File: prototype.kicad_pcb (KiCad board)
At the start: 2 copper layers, 101.5 x 83 mm, 7 parts, among them CON1 SNES-CONN, IC1 SN74LVC4245A, IC2 SN74LVC4245A, IC3 SN74LVC4245A, IC4 SN74LVC4245A

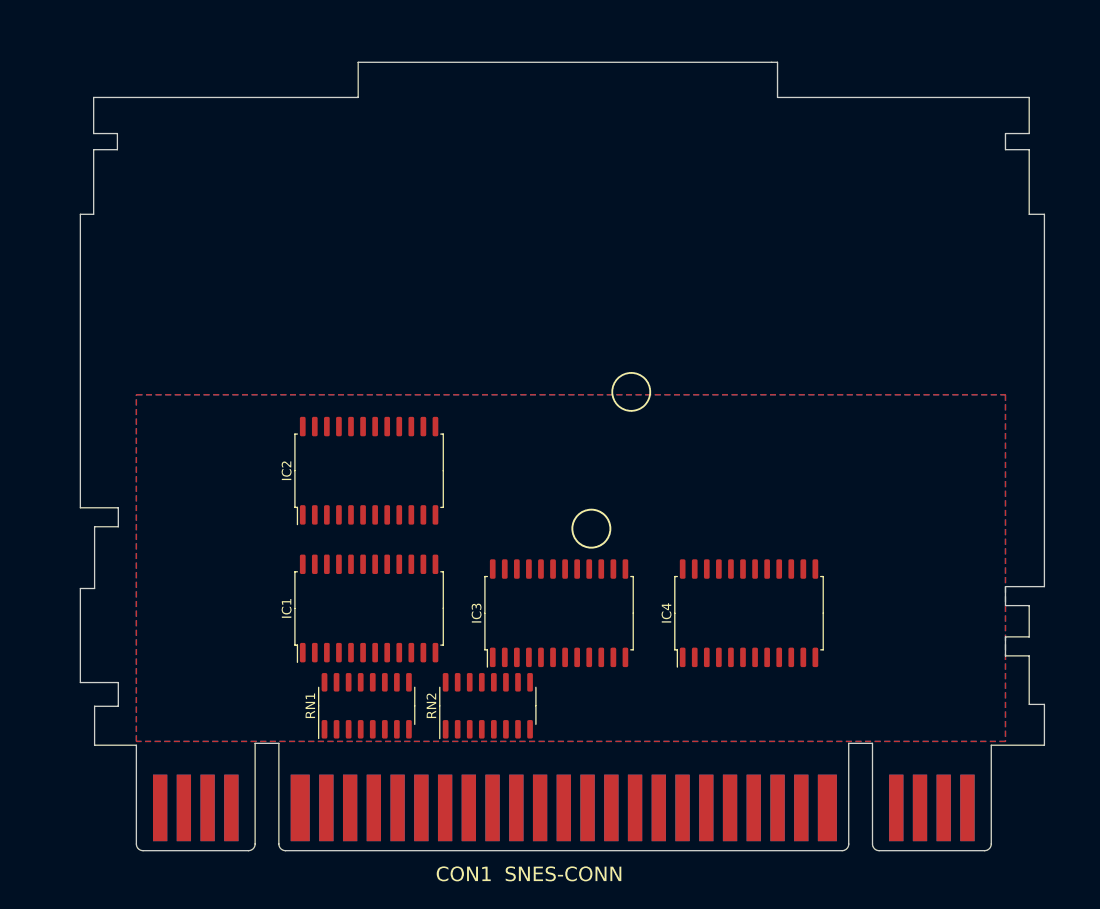
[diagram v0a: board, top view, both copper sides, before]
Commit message: Add resistor networks in between edge connectors and level shifters
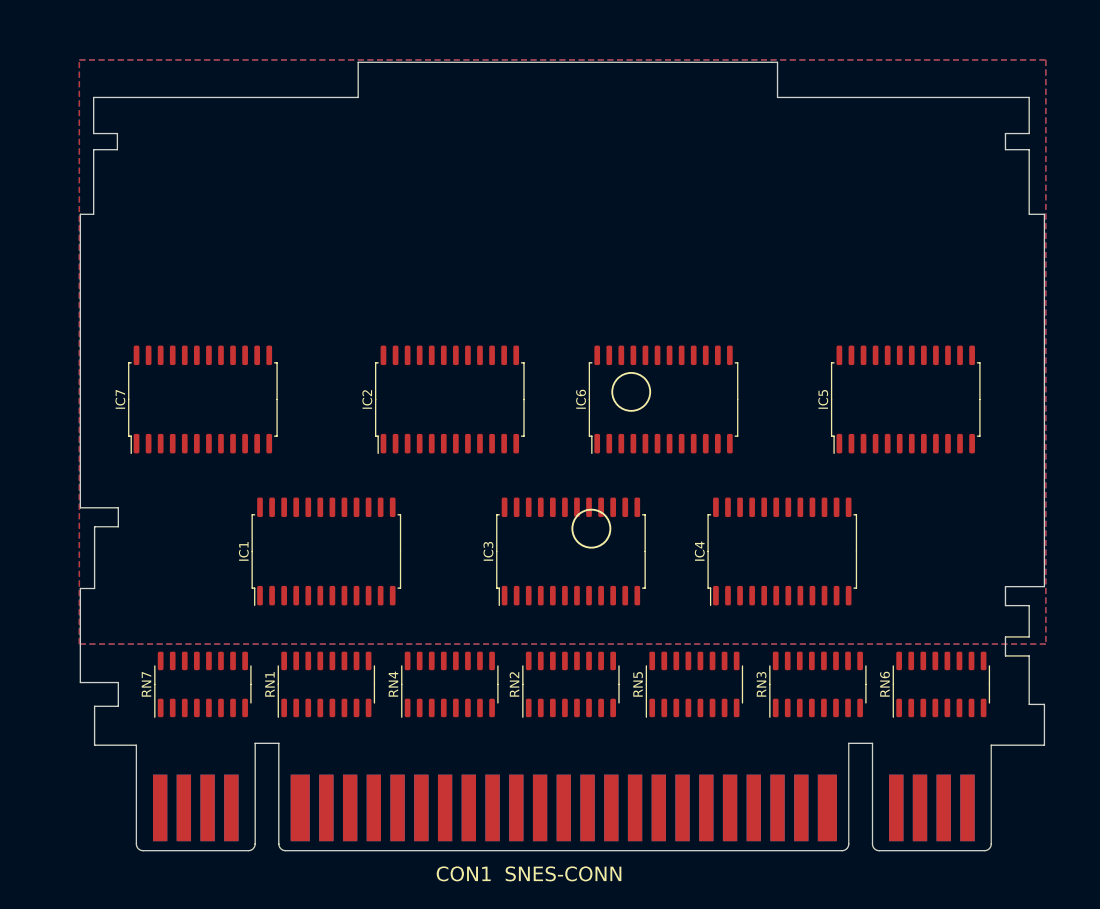
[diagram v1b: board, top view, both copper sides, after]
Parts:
- added IC5: SN74LVC4245A, Package_SO:SOIC-24W_7.5x15.4mm_P1.27mm, F.Cu at (187.0, 87.5)
- added IC6: SN74LVC4245A, Package_SO:SOIC-24W_7.5x15.4mm_P1.27mm, F.Cu at (161.5, 87.5)
- added IC7: SN74LVC4245A, Package_SO:SOIC-24W_7.5x15.4mm_P1.27mm, F.Cu at (113.0, 87.5)
- added RN3: R_Pack08, Package_SO:SOIC-16_3.9x9.9mm_P1.27mm, F.Cu at (177.8, 117.5)
- added RN4: R_Pack08, Package_SO:SOIC-16_3.9x9.9mm_P1.27mm, F.Cu at (139.0, 117.5)
- added RN5: R_Pack08, Package_SO:SOIC-16_3.9x9.9mm_P1.27mm, F.Cu at (164.8, 117.5)
- added RN6: R_Pack08, Package_SO:SOIC-16_3.9x9.9mm_P1.27mm, F.Cu at (190.8, 117.5)
- added RN7: R_Pack08, Package_SO:SOIC-16_3.9x9.9mm_P1.27mm, F.Cu at (113.0, 117.5)
- moved IC2 11.3 mm to (139.0, 87.5)
- moved RN2 9.03 mm to (151.8, 117.5)
- moved IC1 7.50 mm to (126.0, 103.5)
- moved IC4 7.38 mm to (174.0, 103.5)
- moved IC3 6.62 mm to (151.8, 103.5)
- moved RN1 4.81 mm to (126.0, 117.5)
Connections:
- CON1 pad 1: unconnected-(CON1-Pad1) -> Net-(RN7-Pad1)
- CON1 pad 14: A3 -> Net-(CON1-Pad14)
- CON1 pad 15: A2 -> Net-(CON1-Pad15)
- CON1 pad 16: A1 -> Net-(CON1-Pad16)
- CON1 pad 17: A0 -> Net-(CON1-Pad17)
- CON1 pad 18: unconnected-(CON1-Pad18) -> Net-(CON1-Pad18)
- CON1 pad 19: D0 -> Net-(CON1-Pad19)
- CON1 pad 2: unconnected-(CON1-Pad2) -> Net-(RN7-Pad2)
- CON1 pad 20: D1 -> Net-(CON1-Pad20)
- CON1 pad 21: D2 -> Net-(CON1-Pad21)
- CON1 pad 22: D3 -> Net-(CON1-Pad22)
- CON1 pad 23: unconnected-(CON1-Pad23) -> Net-(CON1-Pad23)
- CON1 pad 24: unconnected-(CON1-Pad24) -> Net-(CON1-Pad24)
- CON1 pad 25: unconnected-(CON1-Pad25) -> Net-(CON1-Pad25)
- CON1 pad 26: unconnected-(CON1-Pad26) -> Net-(CON1-Pad26)
- CON1 pad 28: unconnected-(CON1-Pad28) -> Net-(CON1-Pad28)
- CON1 pad 29: unconnected-(CON1-Pad29) -> Net-(CON1-Pad29)
- CON1 pad 3: unconnected-(CON1-Pad3) -> Net-(RN7-Pad3)
- CON1 pad 30: unconnected-(CON1-Pad30) -> Net-(CON1-Pad30)
- CON1 pad 32: unconnected-(CON1-Pad32) -> Net-(RN7-Pad5)
- CON1 pad 33: unconnected-(CON1-Pad33) -> Net-(RN7-Pad6)
- CON1 pad 34: unconnected-(CON1-Pad34) -> Net-(RN7-Pad7)
- CON1 pad 35: unconnected-(CON1-Pad35) -> Net-(RN7-Pad8)
- CON1 pad 4: unconnected-(CON1-Pad4) -> Net-(RN7-Pad4)
- CON1 pad 45: A20 -> Net-(CON1-Pad45)
- CON1 pad 46: A21 -> Net-(CON1-Pad46)
- CON1 pad 47: A22 -> Net-(CON1-Pad47)
- CON1 pad 48: A23 -> Net-(CON1-Pad48)
- CON1 pad 49: unconnected-(CON1-Pad49) -> Net-(CON1-Pad49)
- CON1 pad 50: D4 -> Net-(CON1-Pad50)
- CON1 pad 51: D5 -> Net-(CON1-Pad51)
- CON1 pad 52: D6 -> Net-(CON1-Pad52)
- CON1 pad 53: D7 -> Net-(CON1-Pad53)
- CON1 pad 54: unconnected-(CON1-Pad54) -> Net-(CON1-Pad54)
- CON1 pad 55: unconnected-(CON1-Pad55) -> Net-(CON1-Pad55)
- CON1 pad 56: unconnected-(CON1-Pad56) -> Net-(CON1-Pad56)
- CON1 pad 57: unconnected-(CON1-Pad57) -> Net-(CON1-Pad57)
- CON1 pad 59: unconnected-(CON1-Pad59) -> Net-(CON1-Pad59)
- CON1 pad 60: unconnected-(CON1-Pad60) -> Net-(CON1-Pad60)
- CON1 pad 61: unconnected-(CON1-Pad61) -> Net-(CON1-Pad61)
- IC1 pad 2: A12 -> GND
- IC2 pad 2: unconnected-(IC2-Pad2) -> GND
- IC3 pad 2: unconnected-(IC3-Pad2) -> GND
- RN1 pad 1: A11 -> Net-(CON1-Pad6)
- RN1 pad 10: Net-(CON1-Pad12) -> A5
- RN1 pad 11: Net-(CON1-Pad11) -> A6
- RN1 pad 12: Net-(CON1-Pad10) -> A7
- RN1 pad 13: Net-(CON1-Pad9) -> A8
- RN1 pad 14: Net-(CON1-Pad8) -> A9
- RN1 pad 15: Net-(CON1-Pad7) -> A10
- RN1 pad 16: Net-(CON1-Pad6) -> A11
- RN1 pad 2: A10 -> Net-(CON1-Pad7)
- RN1 pad 3: A9 -> Net-(CON1-Pad8)
- RN1 pad 4: A8 -> Net-(CON1-Pad9)
- RN1 pad 5: A7 -> Net-(CON1-Pad10)
- RN1 pad 6: A6 -> Net-(CON1-Pad11)
- RN1 pad 7: A5 -> Net-(CON1-Pad12)
- RN1 pad 8: A4 -> Net-(CON1-Pad13)
- RN1 pad 9: Net-(CON1-Pad13) -> A4
- RN2 pad 1: Net-(CON1-Pad37) -> Net-(CON1-Pad14)
- RN2 pad 10: A18 -> D1
- RN2 pad 11: A17 -> D0
- RN2 pad 12: A16 -> ~{IRQ}
- RN2 pad 13: A15 -> A0
- RN2 pad 14: A14 -> A1
- RN2 pad 15: A13 -> A2
- RN2 pad 16: A12 -> A3
- RN2 pad 2: Net-(CON1-Pad38) -> Net-(CON1-Pad15)
- RN2 pad 3: Net-(CON1-Pad39) -> Net-(CON1-Pad16)
- RN2 pad 4: Net-(CON1-Pad40) -> Net-(CON1-Pad17)
- RN2 pad 5: Net-(CON1-Pad41) -> Net-(CON1-Pad18)
- RN2 pad 6: Net-(CON1-Pad42) -> Net-(CON1-Pad19)
- RN2 pad 7: Net-(CON1-Pad43) -> Net-(CON1-Pad20)
- RN2 pad 8: Net-(CON1-Pad44) -> Net-(CON1-Pad21)
- RN2 pad 9: A19 -> D2

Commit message: Add 3V3 voltage regulator
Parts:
- added U1: AMS1117-3.3, Package_TO_SOT_SMD:SOT-223-3_TabPin2, F.Cu at (196.0, 101.0)
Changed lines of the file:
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@@
   (net 188 "unconnected-(IC7-Pad23)")
   (net 189 "unconnected-(IC7-Pad24)")
+  (net 190 "3V3")
   (footprint "Package_SO:SOIC-16_3.9x9.9mm_P1.27mm" (layer "F.Cu")
     (at 126 117.5 90)
@@
       (offset (xyz 0 0 0))
       (scale (xyz 1 1 1))
+      (rotate (xyz 0 0 0))
+    )
+  )
+  (footprint "Package_TO_SOT_SMD:SOT-223-3_TabPin2" (layer "F.Cu")
+    (at 196 101)
+    (descr "module CMS SOT223 4 pins")
+    (tags "CMS SOT")
+    (property "Sheetfile" "prototype.kicad_sch")
+    (property "Sheetname" "")
+    (attr smd)
+    (fp_text reference "U1" (at 0 -4.5) (layer "F.SilkS")
+      (effects (font (size 1 1) (thickness 0.15)))
+    )
+    (fp_text value "AMS1117-3.3" (at 0 4.5) (layer "F.Fab")
+      (effects (font (size 1 1) (thickness 0.15)))
+    )
+    (fp_text user "${REFERENCE}" (at 0 0 90) (layer "F.Fab")
+      (effects (font (size 0.8 0.8) (thickness 0.12)))
+    )
+    (fp_line (start 1.91 3.41) (end 1.91 2.15) (layer "F.SilkS") (width 0.12))
+    (fp_line (start -4.1 -3.41) (end 1.91 -3.41) (layer "F.SilkS") (width 0.12))
+    (fp_line (start -1.85 3.41) (end 1.91 3.41) (layer "F.SilkS") (width 0.12))
+    (fp_line (start 1.91 -3.41) (end 1.91 -2.15) (layer "F.SilkS") (width 0.12))
+    (fp_line (start 4.4 3.6) (end 4.4 -3.6) (layer "F.CrtYd") (width 0.05))
+    (fp_line (start -4.4 -3.6) (end -4.4 3.6) (layer "F.CrtYd") (width 0.05))
+    (fp_line (start -4.4 3.6) (end 4.4 3.6) (layer "F.CrtYd") (width 0.05))
+    (fp_line (start 4.4 -3.6) (end -4.4 -3.6) (layer "F.CrtYd") (width 0.05))
+    (fp_line (start -0.85 -3.35) (end 1.85 -3.35) (layer "F.Fab") (width 0.1))
+    (fp_line (start 1.85 -3.35) (end 1.85 3.35) (layer "F.Fab") (width 0.1))
+    (fp_line (start -1.85 -2.35) (end -1.85 3.35) (layer "F.Fab") (width 0.1))
+    (fp_line (start -1.85 -2.35) (end -0.85 -3.35) (layer "F.Fab") (width 0.1))
+    (fp_line (start -1.85 3.35) (end 1.85 3.35) (layer "F.Fab") (width 0.1))
+    (pad "1" smd rect (at -3.15 -2.3) (size 2 1.5) (layers "F.Cu" "F.Paste" "F.Mask")
+      (net 27 "GND") (pinfunction "GND") (pintype "power_in"))
+    (pad "2" smd rect (at -3.15 0) (size 2 1.5) (layers "F.Cu" "F.Paste" "F.Mask")
+      (net 190 "3V3") (pinfunction "VO") (pintype "power_out"))
+    (pad "2" smd rect (at 3.15 0) (size 2 3.8) (layers "F.Cu" "F.Paste" "F.Mask")
+      (net 190 "3V3") (pinfunction "VO") (pintype "power_out"))
+    (pad "3" smd rect (at -3.15 2.3) (size 2 1.5) (layers "F.Cu" "F.Paste" "F.Mask")
+      (net 44 "VCC") (pinfunction "VI") (pintype "power_in"))
+    (model "${KICAD6_3DMODEL_DIR}/Package_TO_SOT_SMD.3dshapes/SOT-223.wrl"
+      (offset (xyz 0 0 0))
+      (scale (xyz 1 1 1))

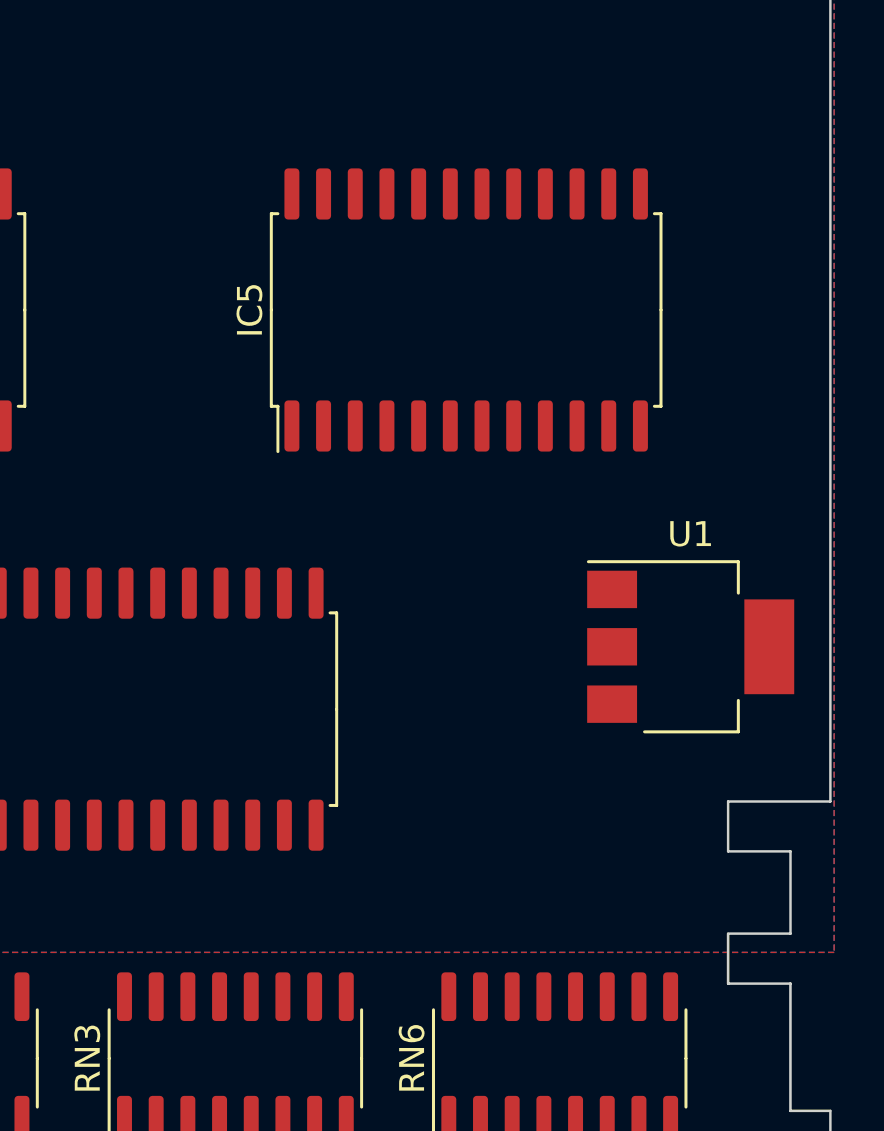
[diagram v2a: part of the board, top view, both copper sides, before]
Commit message: Added 1206 footprints to caps
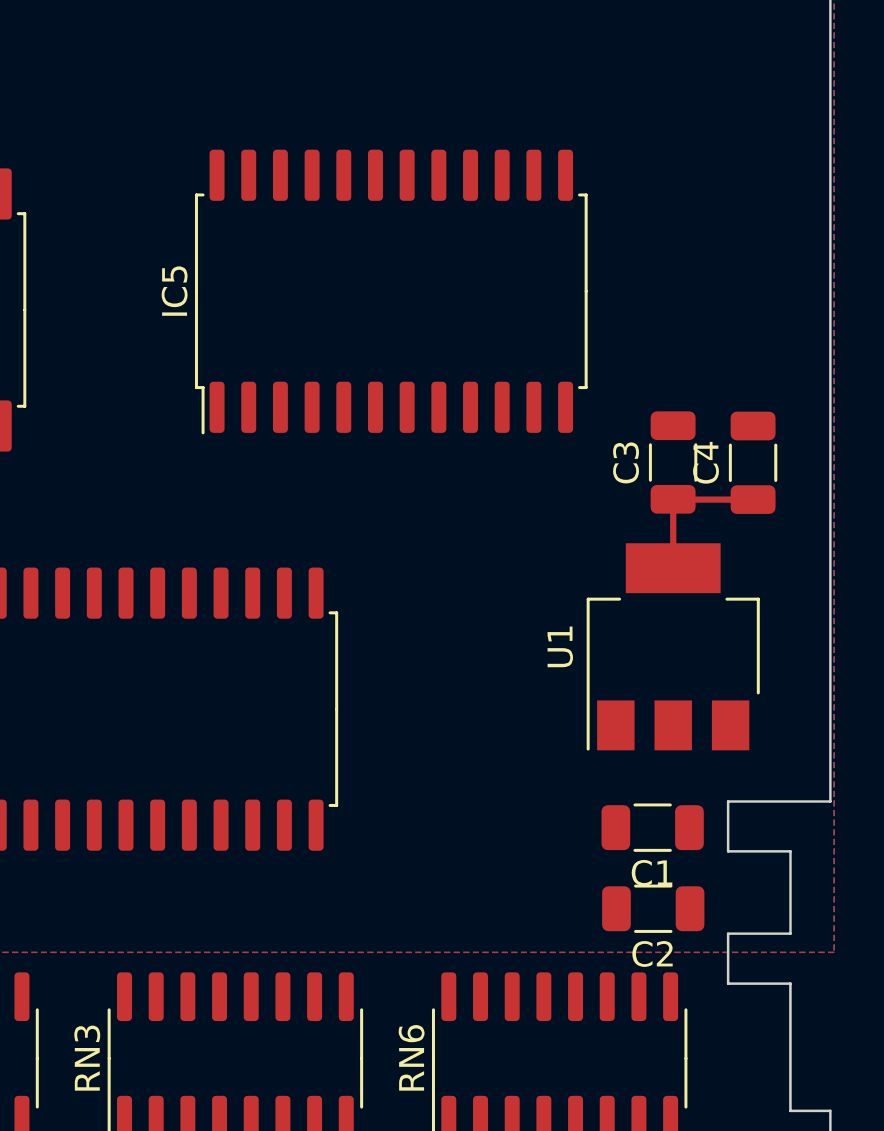
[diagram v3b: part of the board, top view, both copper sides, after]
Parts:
- added C1: 10uF, Capacitor_SMD:C_1206_3216Metric, F.Cu at (194.5, 108.2)
- added C2: 0.1uF, Capacitor_SMD:C_1206_3216Metric, F.Cu at (194.5, 111.5)
- added C3: 10uF, Capacitor_SMD:C_1206_3216Metric, F.Cu at (195.3, 93.6)
- added C4: 0.1uF, Capacitor_SMD:C_1206_3216Metric, F.Cu at (198.5, 93.6)
- moved IC5 3.09 mm to (184.0, 86.8)
- moved U1 0.70 mm to (195.3, 101.0), turned to 90 degrees
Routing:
- net 3V3: track 0.00 -> 5.97 mm
